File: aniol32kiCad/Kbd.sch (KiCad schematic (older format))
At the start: 26 parts

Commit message: lots of changes
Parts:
- removed U? (x2): 74LS14, symbol 74xx:74LS14
- removed U? (x4): 74LS32, symbol 74xx:74LS32
- added C15: 47n, Capacitor_THT:C_Disc_D5.0mm_W2.5mm_P5.00mm, symbol Device:C_Small
- added C16: 10n, Capacitor_THT:C_Disc_D5.0mm_W2.5mm_P5.00mm, symbol Device:C_Small
- added D1: D, Diode_THT:D_5KPW_P7.62mm_Vertical_AnodeUp, symbol Device:D
- added R3: 1M, Resistor_THT:R_Axial_DIN0207_L6.3mm_D2.5mm_P7.62mm_Horizontal, symbol Device:R_Small
- added R4: 20k, Resistor_THT:R_Axial_DIN0207_L6.3mm_D2.5mm_P7.62mm_Horizontal, symbol Device:R_Small
- added unit 4 of U2
- added unit 5 of U2
- added unit 6 of U2
- added U3: 74LS14, Package_DIP:DIP-14_W7.62mm_Socket, symbol 74xx:74LS14
- added U4: 74LS32, Package_DIP:DIP-14_W7.62mm_Socket, symbol 74xx:74LS32
- C17: renamed from C?; value C -> 100n; footprint (none) -> Capacitor_THT:C_Disc_D5.0mm_W2.5mm_P5.00mm
- J5: renamed from J?; footprint (none) -> Connector_PinHeader_2.54mm:PinHeader_1x02_P2.54mm_Vertical
- KBD_CONN1: renamed from J?; footprint (none) -> Connector_PinHeader_2.54mm:PinHeader_1x16_P2.54mm_Vertical
- R10: renamed from R?; value R_Small -> 4k7; footprint (none) -> Resistor_THT:R_Axial_DIN0207_L6.3mm_D2.5mm_P7.62mm_Horizontal
- R5, R6, R7, R8: renamed from R?; value R -> 4k7; footprint (none) -> Resistor_THT:R_Axial_DIN0207_L6.3mm_D2.5mm_P7.62mm_Horizontal
- R9: renamed from R?; value R_Small -> 100k; footprint (none) -> Resistor_THT:R_Axial_DIN0207_L6.3mm_D2.5mm_P7.62mm_Horizontal
- RN1: renamed from RN?; value R_Network08 -> 8x4k7
- U10, U13, U14: renamed from U?; footprint (none) -> Package_DIP:DIP-16_W7.62mm_Socket
- U11: renamed from U?; footprint (none) -> Package_DIP:DIP-20_W7.62mm_Socket
- U12, U2, U5: renamed from U?; footprint (none) -> Package_DIP:DIP-14_W7.62mm_Socket
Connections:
- net +5V: now also U13.12 (I7), U13.13 (I6), U13.14 (I5), U13.15 (I4)
- net A6: now also U4.2
- net GND: now also C15.2, R4.2
- net IORQ: now also U4.1, U4.12
- net M1: now also U4.13
- net RD: now also U4.4
- net WR: now also U4.10
- net at U5.6: now also U2.13
- net at R10.2: now also U2.12
- net at R9.1, U13.5 (Z): now also D1.2 (A)
- net at C17.1, R9.2: now also D1.1 (K), U2.9
- net at U12.3 (C): now also U2.10
- net at U2.5: now also U4.8
- net at U11.1 (OE): now also U4.6
- net at U5.2: now also U4.11
- net IEI renamed KIE
- new net: C15.1, R3.2, U3.1
- new net: C16.2, R3.1, U3.2
- new net: C16.1, R4.1, U3.3
- new net: U2.11, U2.8
- new net: U4.3, U4.5, U4.9
- new net NMI: U3.4
- no-connect marks 10 -> 6

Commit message: added bitmapped text bin file generator
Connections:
- net +5V: now also U12.13 (~R)
- net GND: no longer U12.13 (~R)
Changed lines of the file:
@@
-	1    0    0    -1
-$EndComp
-$Comp
-L power:GND #PWR023
-U 1 1 61B48E69
-P 3300 3550
-F 0 "#PWR023" H 3300 3300 50  0001 C CNN
-F 1 "GND" H 3305 3377 50  0000 C CNN
-F 2 "" H 3300 3550 50  0001 C CNN
-F 3 "" H 3300 3550 50  0001 C CNN
-	1    3300 3550
 	1    0    0    -1
 $EndComp
@@
 Wire Wire Line
 	6800 3800 6700 3800
+$Comp
+L power:+5V #PWR?
+U 1 1 61EA6585
+P 3600 3800
+F 0 "#PWR?" H 3600 3650 50  0001 C CNN
+F 1 "+5V" H 3615 3973 50  0000 C CNN
+F 2 "" H 3600 3800 50  0001 C CNN
+F 3 "" H 3600 3800 50  0001 C CNN
+	1    3600 3800
+	1    0    0    -1
+$EndComp
+Wire Wire Line
+	3600 3800 3600 3950
+Wire Wire Line
+	3600 3950 3300 3950
+Wire Wire Line
+	3300 3950 3300 3550
 $EndSCHEMATC

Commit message: tidied up the PCB
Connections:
- net D0: now also RN1.2 (R1); no longer RN1.9 (R8)
- net D1: now also RN1.3 (R2); no longer RN1.8 (R7)
- net D2: now also RN1.4 (R3); no longer RN1.7 (R6)
- net D3: now also RN1.5 (R4); no longer RN1.6 (R5)
- net D4: now also RN1.6 (R5); no longer RN1.5 (R4)
- net D5: now also RN1.7 (R6); no longer RN1.4 (R3)
- net D6: now also RN1.8 (R7); no longer RN1.3 (R2)
- net D7: now also RN1.9 (R8); no longer RN1.2 (R1)
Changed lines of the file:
@@
 L power:GND #PWR?
 U 1 1 61B2A1CC
-P 7800 2450
+P 7100 2450
 AR Path="/61B2A1CC" Ref="#PWR?"  Part="1"
 AR Path="/61AEA36E/61B2A1CC" Ref="#PWR033"  Part="1"
-F 0 "#PWR033" H 7800 2200 50  0001 C CNN
-F 1 "GND" H 7805 2277 50  0000 C CNN
-F 2 "" H 7800 2450 50  0001 C CNN
-F 3 "" H 7800 2450 50  0001 C CNN
-	1    7800 2450
+F 0 "#PWR033" H 7100 2200 50  0001 C CNN
+F 1 "GND" H 7105 2277 50  0000 C CNN
+F 2 "" H 7100 2450 50  0001 C CNN
+F 3 "" H 7100 2450 50  0001 C CNN
+	1    7100 2450
 	1    0    0    -1
 $EndComp
@@
 L Device:R_Network08 RN1
 U 1 1 61B2A1DA
-P 7400 2250
-F 0 "RN1" V 7925 2250 50  0000 C CNN
-F 1 "8x4k7" V 7834 2250 50  0000 C CNN
-F 2 "Resistor_THT:R_Array_SIP9" V 7875 2250 50  0001 C CNN
-F 3 "http://www.vishay.com/docs/31509/csc.pdf" H 7400 2250 50  0001 C CNN
-	1    7400 2250
-	-1   0    0    1
+P 7500 2250
+F 0 "RN1" V 8025 2250 50  0000 C CNN
+F 1 "8x4k7" V 7934 2250 50  0000 C CNN
+F 2 "Resistor_THT:R_Array_SIP9" V 7975 2250 50  0001 C CNN
+F 3 "http://www.vishay.com/docs/31509/csc.pdf" H 7500 2250 50  0001 C CNN
+	1    7500 2250
+	1    0    0    1
 $EndComp
 Text GLabel 8200 1050 2    50   Input ~ 0
@@
 	6800 3800 6700 3800
 $Comp
-L power:+5V #PWR?
+L power:+5V #PWR0105
 U 1 1 61EA6585
 P 3600 3800
-F 0 "#PWR?" H 3600 3650 50  0001 C CNN
+F 0 "#PWR0105" H 3600 3650 50  0001 C CNN
 F 1 "+5V" H 3615 3973 50  0000 C CNN
 F 2 "" H 3600 3800 50  0001 C CNN

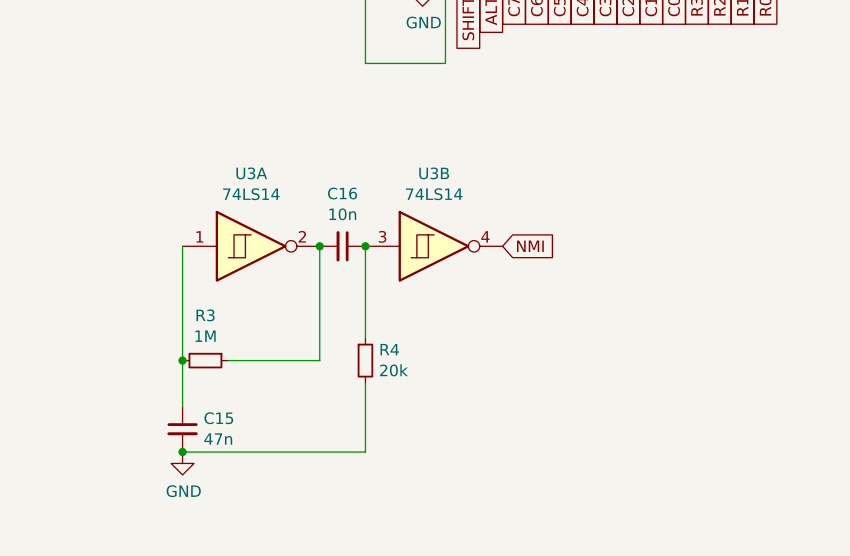
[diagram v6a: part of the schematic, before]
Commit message: Doc changes
Removed a '32 from A32
Documented the VGA connector
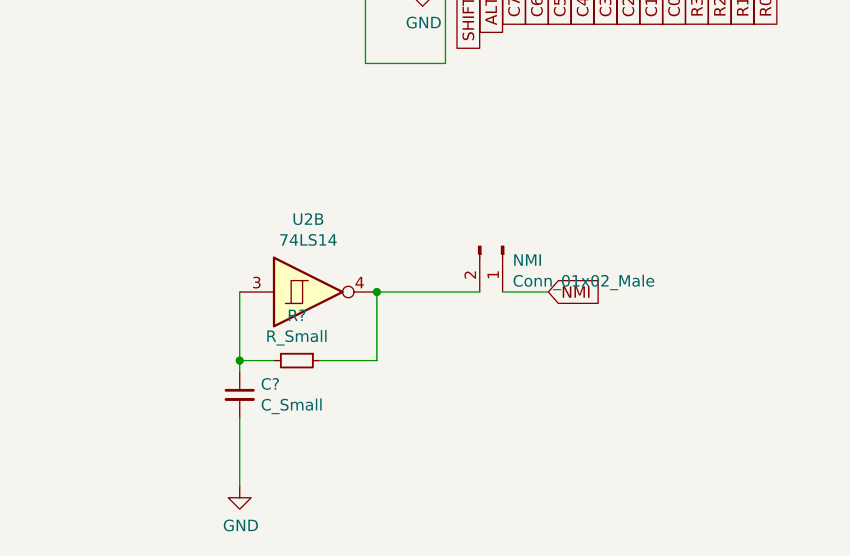
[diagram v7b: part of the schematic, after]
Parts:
- removed C15: 47n, Capacitor_THT:C_Disc_D5.0mm_W2.5mm_P5.00mm, symbol Device:C_Small
- removed C16: 10n, Capacitor_THT:C_Disc_D5.0mm_W2.5mm_P5.00mm, symbol Device:C_Small
- removed R3: 1M, Resistor_THT:R_Axial_DIN0207_L6.3mm_D2.5mm_P7.62mm_Horizontal, symbol Device:R_Small
- removed R4: 20k, Resistor_THT:R_Axial_DIN0207_L6.3mm_D2.5mm_P7.62mm_Horizontal, symbol Device:R_Small
- removed U3: 74LS14, Package_DIP:DIP-14_W7.62mm_Socket, symbol 74xx:74LS14
- added C?: C_Small, symbol Device:C_Small
- added NMI: Conn_01x02_Male, symbol Connector:Conn_01x02_Male
- added R?: R_Small, symbol Device:R_Small
- added unit 2 of U2
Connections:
- net GND: now also C?.2
- net NMI: now also NMI.1 (Pin_1)
- new net: C?.1, R?.2, U2.3
- new net: NMI.2 (Pin_2), R?.1, U2.4
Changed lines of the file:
@@
 NoConn ~ 3600 3350
-$Comp
-L 74xx:74LS14 U3
-U 1 1 61C9A7F9
-P 1900 6500
-F 0 "U3" H 1900 6817 50  0000 C CNN
-F 1 "74LS14" H 1900 6726 50  0000 C CNN
-F 2 "Package_DIP:DIP-14_W7.62mm_Socket" H 1900 6500 50  0001 C CNN
-F 3 "http://www.ti.com/lit/gpn/sn74LS14" H 1900 6500 50  0001 C CNN
-	1    1900 6500
-	1    0    0    -1
-$EndComp
-$Comp
-L 74xx:74LS14 U3
-U 2 1 61C9B9CE
-P 2700 6500
-F 0 "U3" H 2700 6817 50  0000 C CNN
-F 1 "74LS14" H 2700 6726 50  0000 C CNN
-F 2 "Package_DIP:DIP-14_W7.62mm_Socket" H 2700 6500 50  0001 C CNN
-F 3 "http://www.ti.com/lit/gpn/sn74LS14" H 2700 6500 50  0001 C CNN
-	2    2700 6500
-	1    0    0    -1
-$EndComp
-$Comp
-L Device:R_Small R3
-U 1 1 61CA2EF5
-P 1700 7000
-F 0 "R3" V 1504 7000 50  0000 C CNN
-F 1 "1M" V 1595 7000 50  0000 C CNN
-F 2 "Resistor_THT:R_Axial_DIN0207_L6.3mm_D2.5mm_P7.62mm_Horizontal" H 1700 7000 50  0001 C CNN
-F 3 "~" H 1700 7000 50  0001 C CNN
-	1    1700 7000
-	0    1    1    0
-$EndComp
-$Comp
-L Device:R_Small R4
-U 1 1 61CA45D4
-P 2400 7000
-F 0 "R4" H 2459 7046 50  0000 L CNN
-F 1 "20k" H 2459 6955 50  0000 L CNN
-F 2 "Resistor_THT:R_Axial_DIN0207_L6.3mm_D2.5mm_P7.62mm_Horizontal" H 2400 7000 50  0001 C CNN
-F 3 "~" H 2400 7000 50  0001 C CNN
-	1    2400 7000
-	1    0    0    -1
-$EndComp
-$Comp
-L Device:C_Small C15
-U 1 1 61CA48AA
-P 1600 7300
-F 0 "C15" H 1692 7346 50  0000 L CNN
-F 1 "47n" H 1692 7255 50  0000 L CNN
-F 2 "Capacitor_THT:C_Disc_D5.0mm_W2.5mm_P5.00mm" H 1600 7300 50  0001 C CNN
-F 3 "~" H 1600 7300 50  0001 C CNN
-	1    1600 7300
-	1    0    0    -1
-$EndComp
-Wire Wire Line
-	1600 6500 1600 7000
-Connection ~ 1600 7000
-Wire Wire Line
-	1600 7000 1600 7200
-Wire Wire Line
-	2200 6500 2200 7000
-Wire Wire Line
-	2200 7000 1800 7000
-$Comp
-L Device:C_Small C16
-U 1 1 61CB99B3
-P 2300 6500
-F 0 "C16" V 2071 6500 50  0000 C CNN
-F 1 "10n" V 2162 6500 50  0000 C CNN
-F 2 "Capacitor_THT:C_Disc_D5.0mm_W2.5mm_P5.00mm" H 2300 6500 50  0001 C CNN
-F 3 "~" H 2300 6500 50  0001 C CNN
-	1    2300 6500
-	0    1    1    0
-$EndComp
-Connection ~ 2200 6500
-Wire Wire Line
-	2400 6900 2400 6500
-Connection ~ 2400 6500
-Wire Wire Line
-	2400 7100 2400 7400
-Wire Wire Line
-	2400 7400 1600 7400
-$Comp
-L power:GND #PWR019
-U 1 1 61CC603D
-P 1600 7400
-F 0 "#PWR019" H 1600 7150 50  0001 C CNN
-F 1 "GND" H 1605 7227 50  0000 C CNN
-F 2 "" H 1600 7400 50  0001 C CNN
-F 3 "" H 1600 7400 50  0001 C CNN
-	1    1600 7400
-	1    0    0    -1
-$EndComp
-Connection ~ 1600 7400
-Text GLabel 3000 6500 2    50   Input ~ 0
-NMI
 $Comp
 L Device:D D1
@@
 Wire Wire Line
 	3300 3950 3300 3550
+$Comp
+L 74xx:74LS14 U2
+U 2 1 62202FFE
+P 2150 6700
+F 0 "U2" H 2150 7017 50  0000 C CNN
+F 1 "74LS14" H 2150 6926 50  0000 C CNN
+F 2 "" H 2150 6700 50  0001 C CNN
+F 3 "http://www.ti.com/lit/gpn/sn74LS14" H 2150 6700 50  0001 C CNN
+	2    2150 6700
+	1    0    0    -1
+$EndComp
+$Comp
+L Device:C_Small C?
+U 1 1 62207CBA
+P 1850 7150
+F 0 "C?" H 1942 7196 50  0000 L CNN
+F 1 "C_Small" H 1942 7105 50  0000 L CNN
+F 2 "" H 1850 7150 50  0001 C CNN
+F 3 "~" H 1850 7150 50  0001 C CNN
+	1    1850 7150
+	1    0    0    -1
+$EndComp
+Wire Wire Line
+	1850 7050 1850 7000
+$Comp
+L Device:R_Small R?
+U 1 1 6220EC04
+P 2100 7000
+F 0 "R?" V 1904 7000 50  0000 C CNN
+F 1 "R_Small" V 1995 7000 50  0000 C CNN
+F 2 "" H 2100 7000 50  0001 C CNN
+F 3 "~" H 2100 7000 50  0001 C CNN
+	1    2100 7000
+	0    1    1    0
+$EndComp
+Wire Wire Line
+	2200 7000 2450 7000
+Wire Wire Line
+	2450 7000 2450 6700
+Wire Wire Line
+	2000 7000 1850 7000
+Connection ~ 1850 7000
+Wire Wire Line
+	1850 7000 1850 6700
+$Comp
+L power:GND #PWR?
+U 1 1 6221C4C2
+P 1850 7550
+F 0 "#PWR?" H 1850 7300 50  0001 C CNN
+F 1 "GND" H 1855 7377 50  0000 C CNN
+F 2 "" H 1850 7550 50  0001 C CNN
+F 3 "" H 1850 7550 50  0001 C CNN
+	1    1850 7550
+	1    0    0    -1
+$EndComp
+Wire Wire Line
+	1850 7550 1850 7250
+Text GLabel 3200 6700 2    50   Input ~ 0
+NMI
+Connection ~ 2450 6700
+$Comp
+L Connector:Conn_01x02_Male NMI
+U 1 1 6223A9B8
+P 3000 6500
+F 0 "NMI" V 3062 6544 50  0000 L CNN
+F 1 "Conn_01x02_Male" V 3153 6544 50  0000 L CNN
+F 2 "" H 3000 6500 50  0001 C CNN
+F 3 "~" H 3000 6500 50  0001 C CNN
+	1    3000 6500
+	0    1    1    0
+$EndComp
+Wire Wire Line
+	3200 6700 3000 6700
+Wire Wire Line
+	2450 6700 2900 6700
 $EndSCHEMATC
